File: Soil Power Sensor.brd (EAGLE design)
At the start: 100 x 90 mm, 97 parts, among them IC1 TPD2E2U06DCK, J1 12401832E402A, U10 FSA2466, U12 REF2033, U13 TLV1117LV33, U2 FT234XD, U3 MAX9944ATA, U4 ESP32-C3-MINI-1-N4, U5 THS4532, U6 LM27761DSG, U7 INA296A5, U8 MAX11201A, X1 SMA-142-0701-801/806

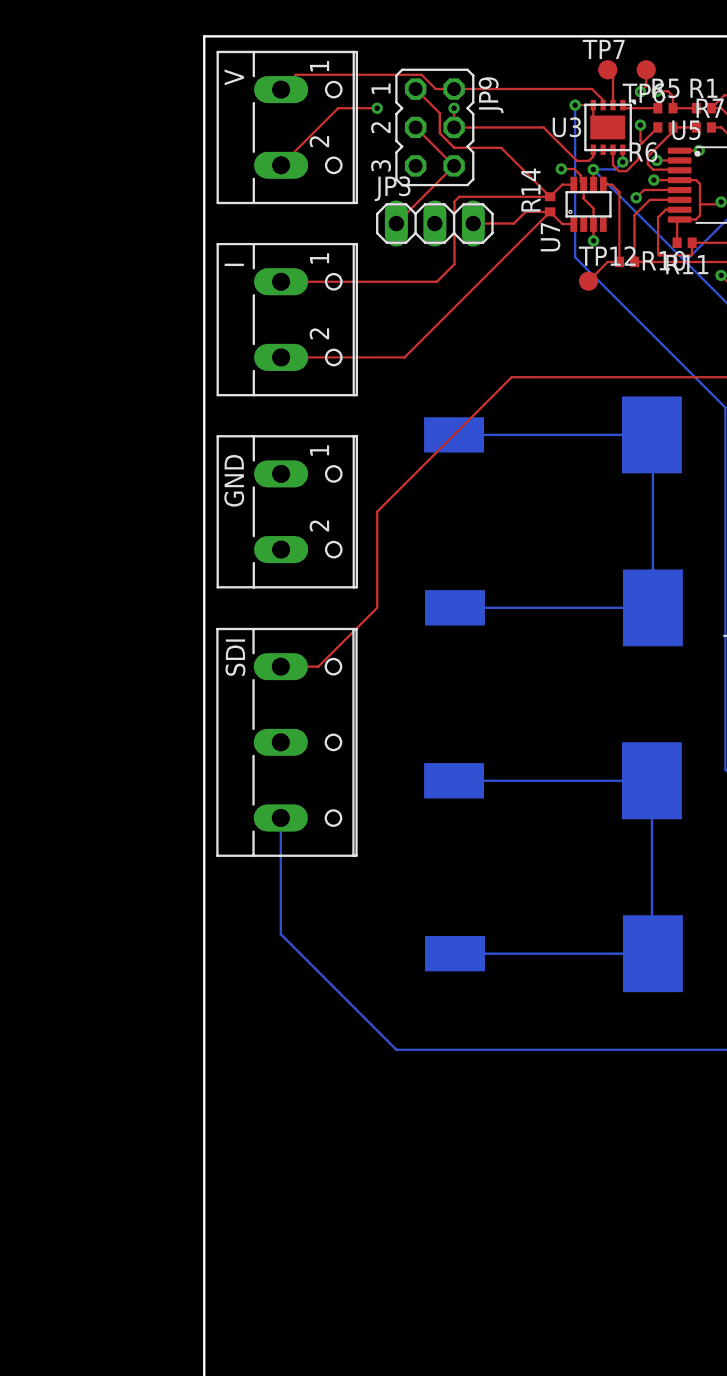
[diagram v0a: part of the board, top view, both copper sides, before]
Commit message: Removed V- buffer and replaced MAX9944 with MAX9943
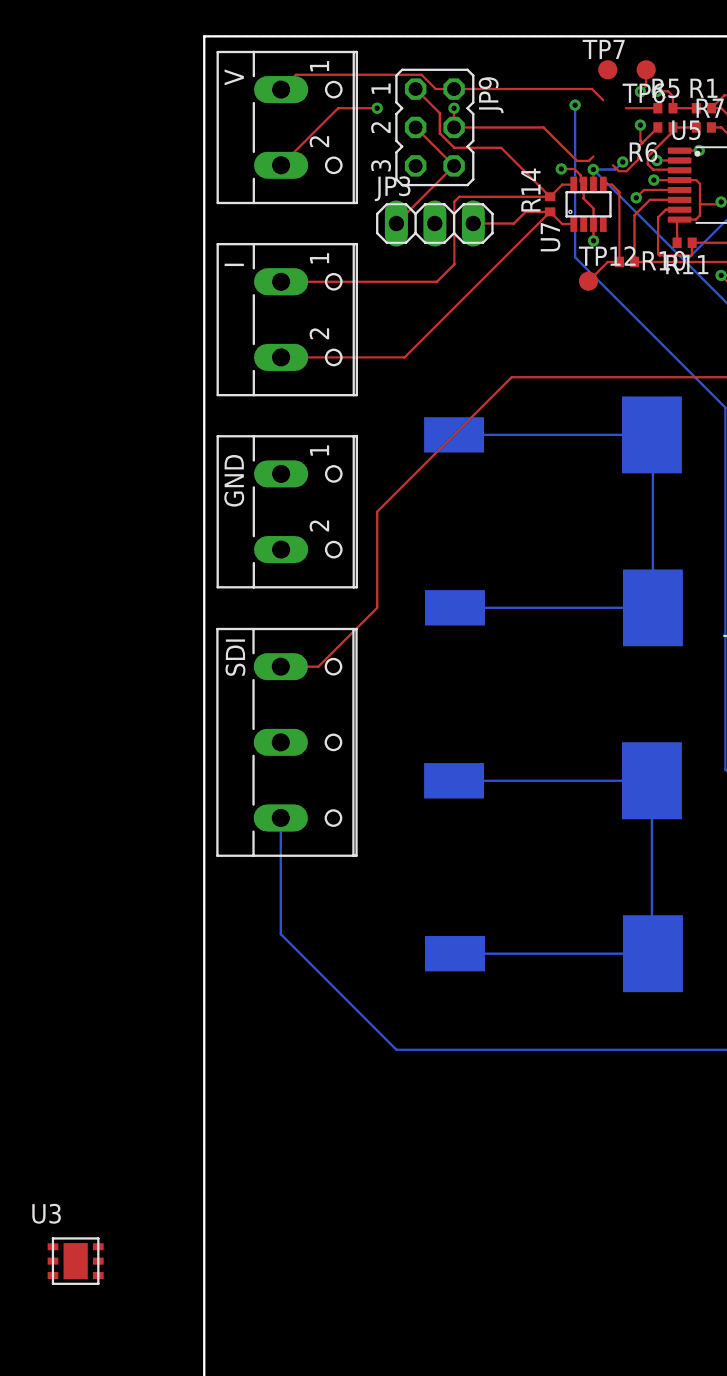
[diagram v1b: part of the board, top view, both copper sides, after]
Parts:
- U3: value MAX9944ATA -> MAX9943ATT+; device Soil Power Sensor:TDFN300X300X75-8N -> Soil Power Sensor:TDFN300X300X75-6N
- moved U3 82.6 mm to (-10.0, 10.0), turned to 0 degrees
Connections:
- removed net N$20: R6.1, TP6.TP, U3.6, U3.7
- removed net N$4: R5.1, TP7.TP, U3.1, U3.2
- new net N$8: R5.1, TP7.TP, U3.1, U3.4
- net +3V3: now also U3.6; no longer U3.8
- net -3V3: now also U3.2; no longer U3.4, U3.9
- net N$46: now also R6.1, TP6.TP; no longer U3.5
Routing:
- net N$20: track 11.5 -> 0.00 mm, vias 2 -> 0
- net N$46: track 24.9 -> 34.4 mm, vias 2 -> 4
- net N$4: track 5.82 -> 0.00 mm
- net -3V3: track 71.5 -> 68.2 mm
- net N$8: track 0.00 -> 2.89 mm
- net +3V3: track 283.8 -> 282.9 mm
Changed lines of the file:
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@@
 <attribute name="VALUE" x="81.3" y="86.21" size="1.27" layer="27" rot="R270" align="top-left"/>
-</element>
-<element name="U3" library="Soil Power Sensor" package="TDFN300X300X75-8N" value="MAX9944ATA" x="26.67" y="83.98" smashed="yes" rot="R270">
-<attribute name="AUTHOR" value="John Madden &lt;jmadden173@pm.me&gt;" x="-57.15" y="24.29" size="1.778" layer="27" rot="R270" display="off"/>
-<attribute name="DATE_CREATED" value="2023-04-05" x="-57.15" y="24.29" size="1.778" layer="27" rot="R270" display="off"/>
-<attribute name="DATE_MODIFIED" value="2023-04-05" x="-57.15" y="24.29" size="1.778" layer="27" rot="R270" display="off"/>
-<attribute name="MFC" value="Analog Devices" x="-57.15" y="24.29" size="1.778" layer="27" rot="R270" display="off"/>
-<attribute name="MPN" value="MAX9944ATA+T" x="-57.15" y="24.29" size="1.778" layer="27" rot="R270" display="off"/>
-<attribute name="NAME" x="22.892" y="83.3544" size="1.27" layer="25"/>
-<attribute name="QTY" value="1" x="-57.15" y="24.29" size="1.778" layer="27" rot="R270" display="off"/>
-<attribute name="REF" value="https://www.analog.com/en/products/max9944.html#product-overview" x="-57.15" y="24.29" size="1.778" layer="27" rot="R270" display="off"/>
-<attribute name="VALUE" x="22.67" y="85.98" size="1.27" layer="27" rot="R270"/>
 </element>
 <element name="U4" library="Soil Power Sensor" package="XCVR_ESP32-C3-MINI-1-N4" value="ESP32-C3-MINI-1-N4" x="96.266" y="12.86" smashed="yes" rot="R270">
@@
 <attribute name="POPULARITY" value="5" x="38.354" y="70.518" size="1.778" layer="27" rot="R180" display="off"/>
 <attribute name="VALUE" x="98.044" y="69.248" size="1.778" layer="27" rot="R180"/>
+</element>
+<element name="U3" library="Soil Power Sensor" package="TDFN300X300X75-6N" value="MAX9943ATT+" x="-10" y="10" smashed="yes">
+<attribute name="AUTHOR" value="John Madden &lt;jmadden173@pm.me&gt;" x="-10" y="10" size="1.778" layer="27" display="off"/>
+<attribute name="DATE_CREATED" value="2023-04-26" x="-10" y="10" size="1.778" layer="27" display="off"/>
+<attribute name="DATE_MODIFIED" value="2023-04-26" x="-10" y="10" size="1.778" layer="27" display="off"/>
+<attribute name="MFC" value="Analog Devices" x="-10" y="10" size="1.778" layer="27" display="off"/>
+<attribute name="MPN" value="MAX9943ATT+T" x="-10" y="10" size="1.778" layer="27" display="off"/>
+<attribute name="NAME" x="-11.5" y="11.548" size="1.27" layer="25"/>
+<attribute name="REF" value="https://www.analog.com/en/products/MAX9943.html" x="-10" y="10" size="1.778" layer="27" display="off"/>
+<attribute name="VALUE" x="-11.524" y="5.555" size="1.27" layer="27"/>
 </element>
 </elements>
@@
 <wire x1="37.16" y1="79.845" x2="37.16" y2="82.445" width="0" layer="19" extent="1-1"/>
 </signal>
-<signal name="N$4">
-<contactref element="U3" pad="2"/>
-<contactref element="U3" pad="1"/>
-<contactref element="R5" pad="1"/>
-<contactref element="TP7" pad="TP"/>
-<wire x1="27.015" y1="85.455" x2="27.665" y2="85.455" width="0.1524" layer="1"/>
-<wire x1="29.775" y1="85.455" x2="29.98" y2="85.25" width="0.1524" layer="1"/>
-<wire x1="29.98" y1="85.25" x2="27.87" y2="85.25" width="0.1524" layer="1"/>
-<wire x1="27.87" y1="85.25" x2="27.665" y2="85.455" width="0.1524" layer="1"/>
-<wire x1="26.67" y1="87.79" x2="27.015" y2="87.445" width="0.1524" layer="1"/>
-<wire x1="27.015" y1="87.445" x2="27.015" y2="85.455" width="0.1524" layer="1"/>
-</signal>
-<signal name="N$20">
-<contactref element="U3" pad="6"/>
-<contactref element="U3" pad="7"/>
-<contactref element="R6" pad="1"/>
-<contactref element="TP6" pad="TP"/>
-<wire x1="26.365" y1="82.505" x2="27.015" y2="82.505" width="0.1524" layer="1"/>
-<wire x1="28.702" y1="82.702" x2="28.96" y2="82.96" width="0.1524" layer="1"/>
-<wire x1="28.96" y1="82.96" x2="29.98" y2="83.98" width="0.1524" layer="1"/>
-<wire x1="27.40925" y1="81.0872" x2="27.91195" y2="81.0872" width="0.1524" layer="1"/>
-<wire x1="27.015" y1="81.48145" x2="27.40925" y2="81.0872" width="0.1524" layer="1"/>
-<wire x1="27.91195" y1="81.0872" x2="28.702" y2="81.87725" width="0.1524" layer="1"/>
-<wire x1="27.015" y1="82.505" x2="27.015" y2="81.48145" width="0.1524" layer="1"/>
-<wire x1="28.702" y1="81.87725" x2="28.702" y2="82.702" width="0.1524" layer="1"/>
-<wire x1="29.21" y1="87.79" x2="29.21" y2="86.7232" width="0.1524" layer="1"/>
-<wire x1="29.21" y1="86.7232" x2="28.829" y2="86.3422" width="0.1524" layer="1"/>
-<via x="28.829" y="86.3422" extent="1-16" drill="0.35"/>
-<wire x1="28.829" y1="86.3422" x2="28.829" y2="84.1324" width="0.1524" layer="15"/>
-<via x="28.829" y="84.1324" extent="1-16" drill="0.35"/>
-<wire x1="28.829" y1="84.1324" x2="28.829" y2="83.091" width="0.1524" layer="1"/>
-<wire x1="28.829" y1="83.091" x2="28.96" y2="82.96" width="0.1524" layer="1"/>
-</signal>
 <signal name="+3V3">
 <contactref element="U7" pad="6"/>
-<contactref element="U3" pad="8"/>
 <contactref element="U5" pad="9"/>
 <contactref element="U5" pad="13"/>
@@
 <wire x1="25.725" y1="81.201425" x2="25.714775" y2="81.201425" width="0.1524" layer="1"/>
 <via x="25.714775" y="81.201425" extent="1-16" drill="0.35"/>
-<wire x1="27.665" y1="82.505" x2="27.665" y2="81.6984" width="0.1524" layer="1"/>
 <wire x1="27.665" y1="81.6984" x2="27.6606" y2="81.694" width="0.1524" layer="1"/>
 <via x="27.6606" y="81.694" extent="1-16" drill="0.35"/>
@@
 <wire x1="80.2132" y1="11.4376" x2="78.1558" y2="9.3802" width="0.1524" layer="16"/>
 <wire x1="78.1558" y1="9.3802" x2="75.09951875" y2="9.3802" width="0.1524" layer="16"/>
+<contactref element="U3" pad="6"/>
+<wire x1="-7" y1="10" x2="36.576" y2="51.468" width="0" layer="19" extent="1-1"/>
 </signal>
 <signal name="REF+1V65">
@@
 </signal>
 <signal name="-3V3">
-<contactref element="U3" pad="4"/>
-<contactref element="U3" pad="9"/>
 <contactref element="U6" pad="4"/>
 <contactref element="C19" pad="1"/>
@@
 <wire x1="34.4424" y1="41.5366" x2="34.4424" y2="65.4634" width="0.1524" layer="16"/>
 <wire x1="34.4424" y1="65.4634" x2="24.511" y2="75.3948" width="0.1524" layer="16"/>
-<wire x1="25.715" y1="85.455" x2="24.5128" y2="85.455" width="0.1524" layer="1"/>
-<wire x1="26.665" y1="83.98" x2="26.305" y2="83.98" width="0.1524" layer="1"/>
-<wire x1="26.305" y1="83.98" x2="25.715" y2="84.57" width="0.1524" layer="1"/>
-<wire x1="25.715" y1="84.57" x2="25.715" y2="85.455" width="0.1524" layer="1"/>
+<contactref element="U3" pad="2"/>
+<wire x1="-10" y1="9.05" x2="38.862" y2="32.418" width="0" layer="19" extent="1-1"/>
 </signal>
 <signal name="PB13/SPI2_SCK">
@@
 </signal>
 <signal name="N$1">
-<contactref element="U3" pad="3"/>
 <contactref element="V" pad="1"/>
 <contactref element="JP9" pad="2"/>
-<wire x1="26.365" y1="85.7836" x2="26.365" y2="85.455" width="0.1524" layer="1"/>
 <wire x1="16.51" y1="86.52" x2="25.6286" y2="86.52" width="0.1524" layer="1"/>
 <wire x1="25.6286" y1="86.52" x2="26.365" y2="85.7836" width="0.1524" layer="1"/>
@@
 <wire x1="5.08" y1="86.48" x2="6.0598" y2="87.4598" width="0.1524" layer="1"/>
 <wire x1="6.0598" y1="87.4598" x2="14.35928125" y2="87.4598" width="0.1524" layer="1"/>
+<contactref element="U3" pad="3"/>
+<wire x1="-10" y1="8.1" x2="5.08" y2="86.48" width="0" layer="19" extent="1-1"/>
 </signal>
 <signal name="N$46">
-<contactref element="U3" pad="5"/>
 <contactref element="JP9" pad="4"/>
 <contactref element="V" pad="2"/>
@@
 <wire x1="24.638" y1="81.7702" x2="25.4254" y2="81.7702" width="0.1524" layer="1"/>
 <wire x1="25.4254" y1="81.7702" x2="25.715" y2="82.0598" width="0.1524" layer="1"/>
-<wire x1="25.715" y1="82.0598" x2="25.715" y2="82.505" width="0.1524" layer="1"/>
 <wire x1="5.08" y1="81.48" x2="8.85" y2="85.25" width="0.1524" layer="1"/>
 <wire x1="8.85" y1="85.25" x2="11.43" y2="85.25" width="0.1524" layer="1"/>
@@
 <via x="16.51" y="85.25" extent="1-16" drill="0.35"/>
 <wire x1="16.51" y1="85.25" x2="16.51" y2="83.98" width="0.1524" layer="1"/>
+<contactref element="R6" pad="1"/>
+<contactref element="TP6" pad="TP"/>
+<wire x1="28.702" y1="82.702" x2="28.96" y2="82.96" width="0.1524" layer="1"/>
+<wire x1="28.96" y1="82.96" x2="29.98" y2="83.98" width="0.1524" layer="1"/>
+<wire x1="27.40925" y1="81.0872" x2="27.91195" y2="81.0872" width="0.1524" layer="1"/>
+<wire x1="27.015" y1="81.48145" x2="27.40925" y2="81.0872" width="0.1524" layer="1"/>
+<wire x1="27.91195" y1="81.0872" x2="28.702" y2="81.87725" width="0.1524" layer="1"/>
+<wire x1="28.702" y1="81.87725" x2="28.702" y2="82.702" width="0.1524" layer="1"/>
+<wire x1="29.21" y1="87.79" x2="29.21" y2="86.7232" width="0.1524" layer="1"/>
+<wire x1="29.21" y1="86.7232" x2="28.829" y2="86.3422" width="0.1524" layer="1"/>
+<via x="28.829" y="86.3422" extent="1-16" drill="0.35"/>
+<wire x1="28.829" y1="86.3422" x2="28.829" y2="84.1324" width="0.1524" layer="15"/>
+<via x="28.829" y="84.1324" extent="1-16" drill="0.35"/>
+<wire x1="28.829" y1="84.1324" x2="28.829" y2="83.091" width="0.1524" layer="1"/>
+<wire x1="28.829" y1="83.091" x2="28.96" y2="82.96" width="0.1524" layer="1"/>
+<wire x1="25.715" y1="82.0598" x2="27.015" y2="81.48145" width="0" layer="19" extent="1-1"/>
 </signal>
 <signal name="N$48">
@@
 <wire x1="60.2606" y1="22.6" x2="82.55" y2="22.6" width="0.1524" layer="1"/>
 </signal>
+<signal name="N$8">
+<contactref element="U3" pad="4"/>
+<contactref element="U3" pad="1"/>
+<contactref element="R5" pad="1"/>
+<contactref element="TP7" pad="TP"/>
+<wire x1="29.775" y1="85.455" x2="29.98" y2="85.25" width="0.1524" layer="1"/>
+<wire x1="29.98" y1="85.25" x2="27.87" y2="85.25" width="0.1524" layer="1"/>
+<wire x1="26.67" y1="87.79" x2="27.015" y2="87.445" width="0.1524" layer="1"/>
+<wire x1="27.87" y1="85.25" x2="27.015" y2="87.445" width="0" layer="19" extent="1-1"/>
+<wire x1="-10" y1="10" x2="27.87" y2="85.25" width="0" layer="19" extent="1-1"/>
+<wire x1="-7" y1="8.1" x2="-10" y2="10" width="0" layer="19" extent="1-1"/>
+</signal>
 </signals>
